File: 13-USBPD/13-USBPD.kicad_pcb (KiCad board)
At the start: 2 copper layers, 43.7 x 25 mm, 34 parts, among them J1 USB_C_Receptacle, Q1 STL6P3LLH6, U1 STUSB4500QTR

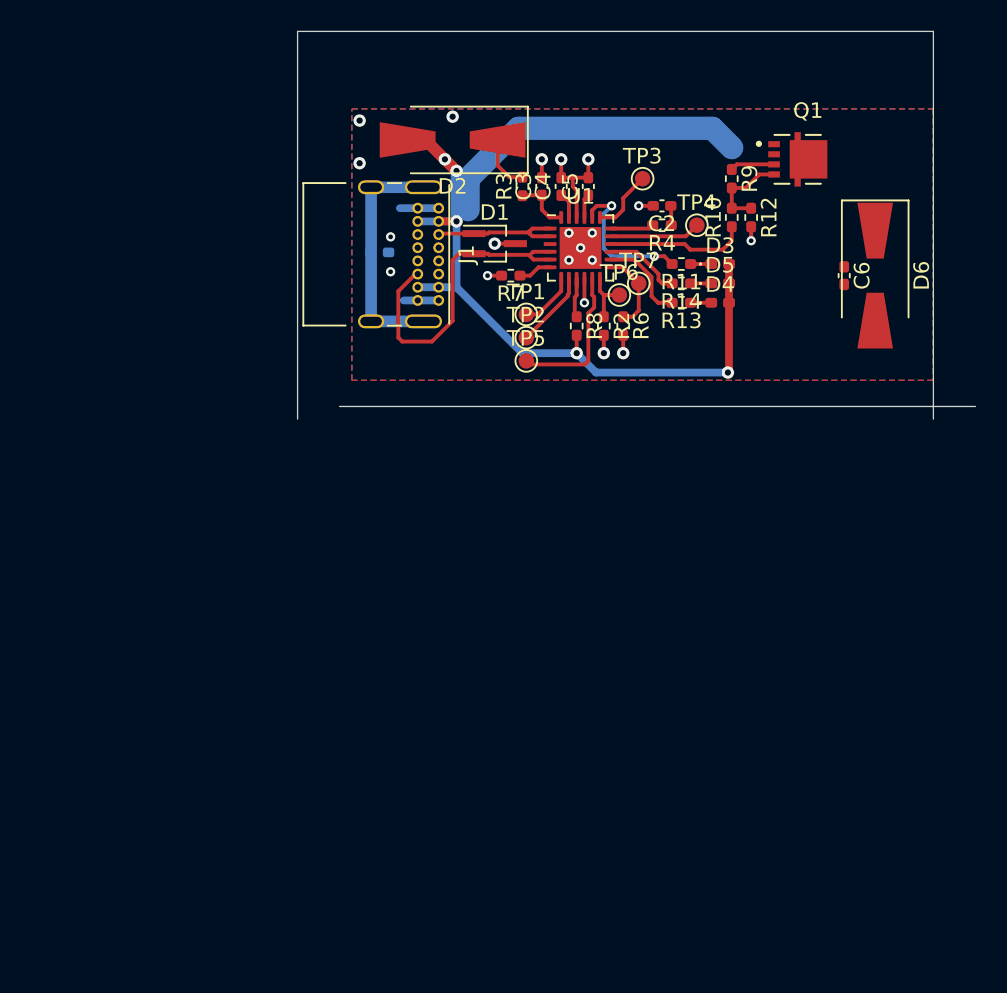
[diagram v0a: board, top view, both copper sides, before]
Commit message: Day 15: Add powerpole outputs, test points, check SCH. Needs some DRC love, mostly courtyard of testpoint violations at the moments.
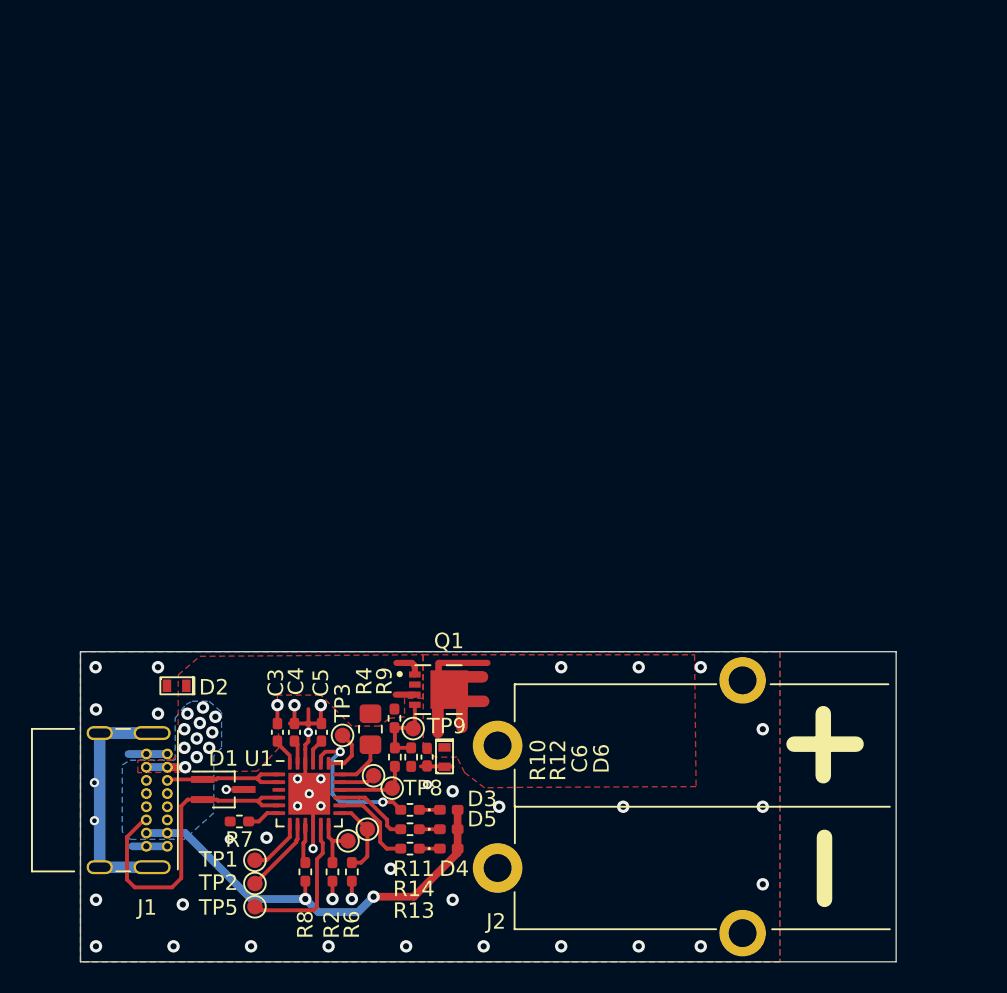
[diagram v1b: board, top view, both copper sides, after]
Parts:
- removed C1: 100nF, Capacitor_SMD:C_0402_1005Metric_Pad0.74x0.62mm_HandSolder
- removed C2: 1uF, Capacitor_SMD:C_0402_1005Metric_Pad0.74x0.62mm_HandSolder
- removed R3: 470, Resistor_SMD:R_0402_1005Metric_Pad0.72x0.64mm_HandSolder
- added J2: Conn_01x02_Female, 13-USBPD:PowerPole_Horizontal_1x2_with_staple, F.Cu at (126.9, 100.0)
- added TP8: TestPoint, TestPoint:TestPoint_Pad_D1.0mm, F.Cu at (120.1, 98.8)
- added TP9: TestPoint, TestPoint:TestPoint_Pad_D1.0mm, F.Cu at (121.5, 95.0)
- D2: value 22V -> ESDA25P35; footprint Diode_SMD:D_SMA-SMB_Universal_Handsoldering -> 13-USBPD:DIODE_SMD_1610
- D6: value D_Zener_Small -> ESDA25P35; footprint Diode_SMD:D_SMA-SMB_Universal_Handsoldering -> 13-USBPD:DIODE_SMD_1610
- R4: footprint Resistor_SMD:R_0402_1005Metric_Pad0.72x0.64mm_HandSolder -> Resistor_SMD:R_0805_2012Metric_Pad1.20x1.40mm_HandSolder
- moved D6 41.7 mm to (123.5, 96.8)
- moved Q1 41.3 mm to (123.1, 92.4)
- moved TP4 41.2 mm to (118.9, 98.0)
- moved R12 41.1 mm to (121.3, 96.8)
- moved C6 41.1 mm to (122.3, 96.8)
- moved R9 41.0 mm to (120.2, 94.3)
- moved R10 41.0 mm to (120.3, 96.8)
- moved TP3 40.8 mm to (116.9, 95.4)
- moved D2 39.4 mm to (106.2, 92.2)
- moved D1 39.3 mm to (109.2, 98.9)
- moved D3 39.3 mm to (123.8, 100.2)
- moved D4 39.3 mm to (123.8, 102.7)
- moved D5 39.3 mm to (123.8, 101.5)
- moved R11 39.3 mm to (121.2, 100.2)
- moved R13 39.3 mm to (121.2, 102.7)
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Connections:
- net Net-(J1-PadA6) renamed no_connect_30
- net Net-(J1-PadA7) renamed no_connect_31
- net Net-(J1-PadA8) renamed no_connect_32
- net Net-(J1-PadB6) renamed no_connect_37
- net Net-(J1-PadB7) renamed no_connect_38
- net Net-(J1-PadB8) renamed no_connect_39
- net no_connect_42 renamed no_connect_40
- D2 pad 1: Net-(C2-Pad1) -> /VBUS
- D2 pad 2: /VBUS -> GND
- J1 pad S1: Net-(C1-Pad1) -> GND
- R4 pad 1: Net-(C2-Pad1) -> /VBUS
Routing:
- net /VBUS: track 73.1 -> 35.8 mm, vias 5 -> 13
- net GND: track 20.5 -> 40.5 mm, vias 20 -> 44
- net /VOUT: track 0.00 -> 16.5 mm
- net Net-(C1-Pad1): track 15.4 -> 0.00 mm
- net Net-(C2-Pad1): track 4.82 -> 0.00 mm
- net Net-(R10-Pad1): track 9.08 -> 4.91 mm
- net Net-(TP4-Pad1): track 6.08 -> 2.36 mm
- net Net-(TP3-Pad1): track 4.22 -> 3.26 mm
- net Net-(R4-Pad2): track 2.78 -> 3.37 mm
- added copper zone on B.Cu, net /VBUS
- added copper zone on F.Cu, net /VBUS
- added copper zone on F.Cu, net /VOUT
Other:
- board size 43.7 x 25 mm -> 52.6 x 20 mm
